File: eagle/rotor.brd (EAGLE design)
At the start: 72.1 x 80 mm, 53 parts, among them IC1 TXS0108, IC2 7815TV, J1 PL9823, J2 pwr2, J3 Power, J4 Antenna, J5 Power, J6 CCW, J7 Brake, J8 CW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

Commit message: eagle
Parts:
- J4: device TB004-508-02BE:CUI_TB004-508-02BE -> TB004-508-03BE:CUI_TB004-508-03BE
- Q1, T1: device test:TO92-EBC-OVAL -> test:TO92-CBE-OVAL
- R3: value 1100 -> 1100 Ω
- moved C4 7.41 mm to (63.5, 63.5)
- moved U3 6.35 mm to (62.2, 69.8)
- moved D1 6.35 mm to (62.2, 43.2), turned to 270 degrees
- moved J5 5.68 mm to (69.8, 12.7)
- moved J9 5.68 mm to (69.8, 22.9)
- moved R3 5.68 mm to (69.8, 64.8)
- moved T1 5.68 mm to (49.5, 19.1), turned to 270 degrees
- moved C5 4.58 mm to (66.0, 50.8)
- moved J7 3.81 mm to (49.5, 5.08)
- moved J1 3.81 mm to (24.1, 5.08)
- moved J6 3.81 mm to (59.7, 5.08)
- moved J8 3.81 mm to (39.4, 5.08)
- moved C1 3.59 mm to (54.6, 68.6)
- moved C3 3.59 mm to (54.6, 64.8)
- moved J3 3.59 mm to (22.9, 72.4)
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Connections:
- net +5V: now also Q1.C; no longer Q1.E
- net GND: now also J4.3
- net N$8: now also Q1.E; no longer Q1.C
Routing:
- net GND: track 241.7 -> 199.1 mm, vias 12 -> 11
- net N$1: track 33.7 -> 29.2 mm
- net SW1-POWER: track 60.2 -> 55.9 mm
- net ROTOR-PWR-LED-SOURCE: track 48.5 -> 44.1 mm
- net ROOF-3: track 23.2 -> 26.6 mm
- net SW4-CW: track 38.8 -> 36.1 mm
- net PL9823-SOURCE: track 37.0 -> 35.3 mm
- net +24: track 27.0 -> 28.5 mm
- net N$3: track 5.82 -> 7.18 mm
- net ROOF-4: track 23.4 -> 24.4 mm
- net SW3-BRAKE: track 42.2 -> 43.2 mm
- net CH0: track 34.3 -> 33.5 mm
- net POWER-OUT: track 51.6 -> 50.8 mm
- net +15V: track 32.3 -> 32.8 mm
- net SW2-CCW: track 52.0 -> 51.5 mm
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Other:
- board size 72.1 x 80 mm -> 74.9 x 77.5 mm

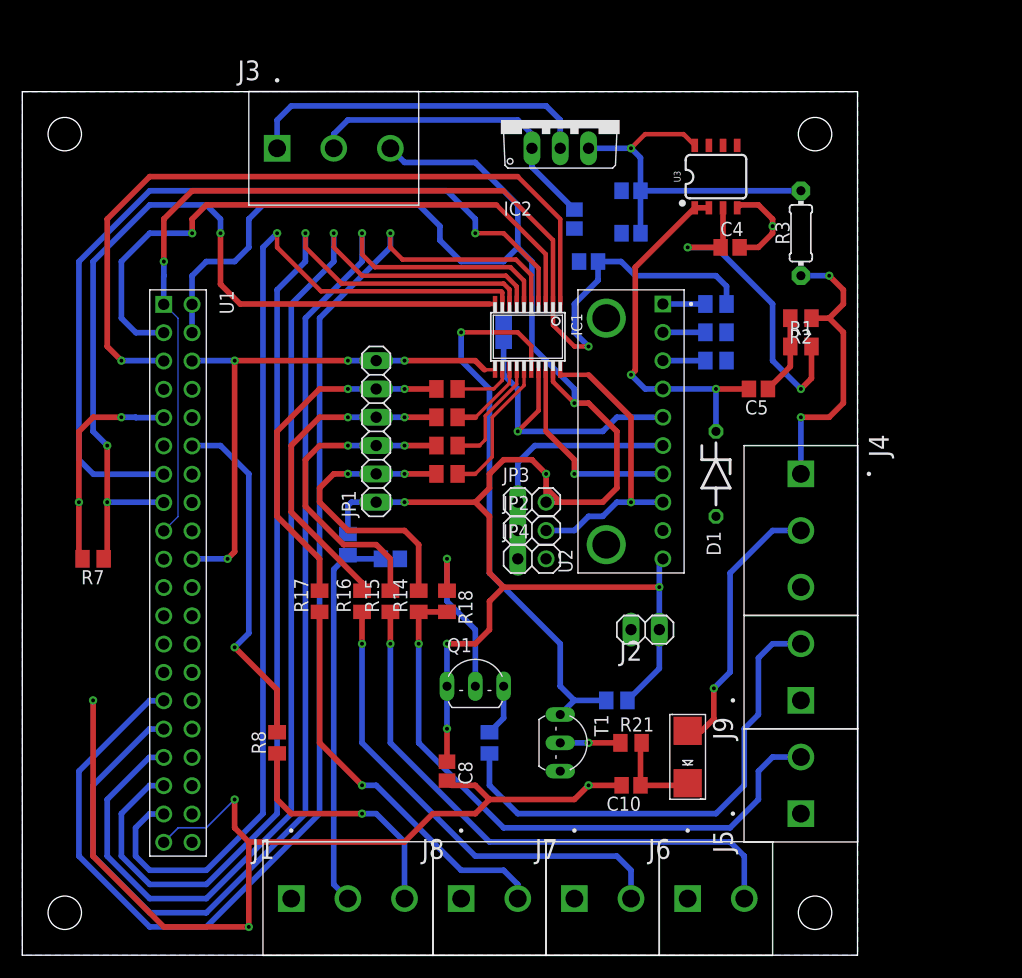
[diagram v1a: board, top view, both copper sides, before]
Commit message: add dpdt switch
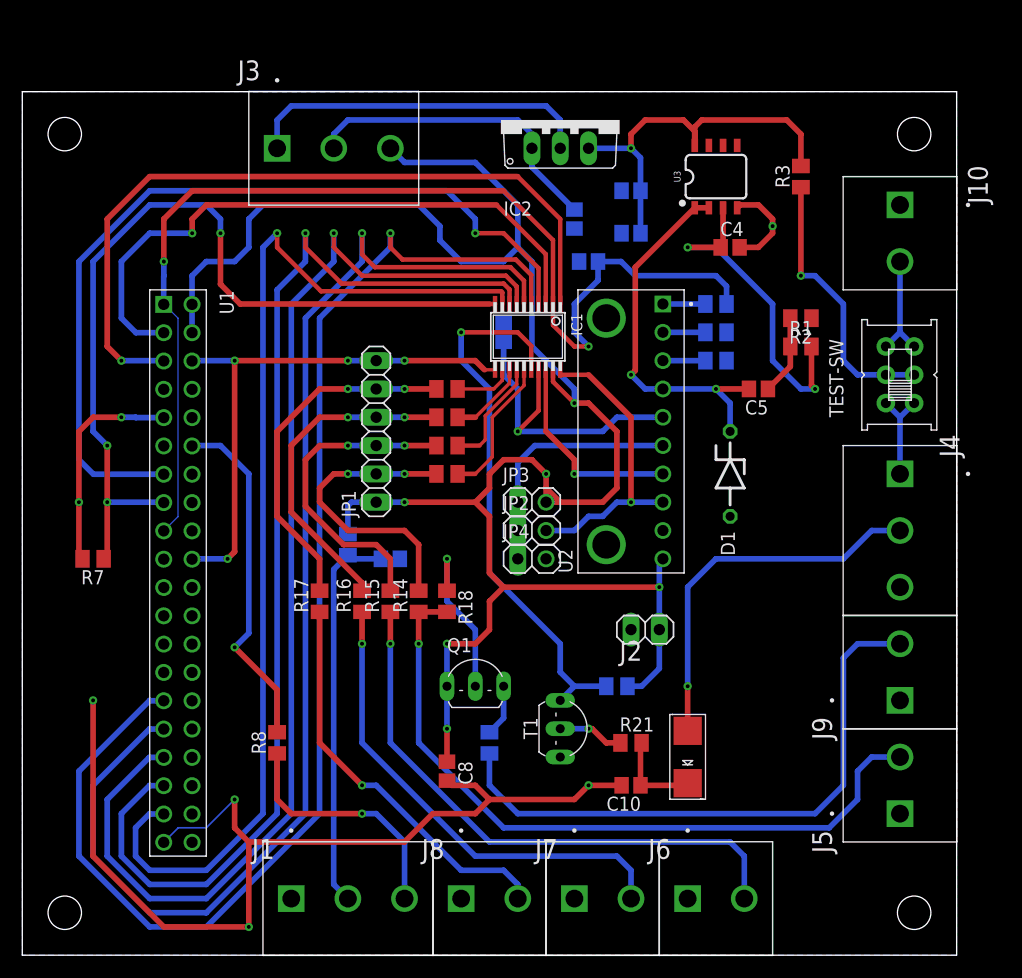
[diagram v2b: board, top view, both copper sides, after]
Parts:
- added J10: TB004-508-02BE, TB004-508-02BE:CUI_TB004-508-02BE
- added TEST-SW: DPDT-SWITCH, ladyada:DP-DT
- R3: device test:0204/7 -> ladyada:M0805
- moved J4 8.89 mm to (78.7, 43.2)
- moved J5 8.89 mm to (78.7, 12.7)
- moved J9 8.89 mm to (78.7, 22.9)
- moved R3 5.08 mm to (69.8, 69.8)
- moved D1 1.27 mm to (63.5, 43.2)
- moved R20 1.27 mm to (53.3, 24.1)
- moved T1 1.27 mm to (49.5, 20.3)
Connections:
- new net N$13: R3.1, TEST-SW.C-1, TEST-SW.C-2
- new net N$14: J10.2, TEST-SW.NC-1, TEST-SW.NC-2
- net GND: now also J10.1
- net ROOF-3: now also TEST-SW.NO-1, TEST-SW.NO-2; no longer R2.1, R3.1
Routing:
- net N$13: track 0.00 -> 24.8 mm, vias 0 -> 1
- net ROOF-3: track 26.6 -> 8.67 mm, vias 2 -> 0
- net N$14: track 0.00 -> 9.94 mm
- net ROTOR-PWR-LED-SOURCE: track 44.1 -> 53.8 mm
- net ROOF-4: track 24.4 -> 34.0 mm
- net SW1-POWER: track 55.9 -> 64.7 mm
- net +15V: track 32.8 -> 35.8 mm
- net POWER-OUT: track 50.8 -> 49.6 mm
- net N$1: track 29.2 -> 30.2 mm
- net CH0: track 33.5 -> 34.1 mm
- net +5V: track 179.4 -> 178.9 mm
- net N$12: track 5.40 -> 5.93 mm
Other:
- board size 74.9 x 77.5 mm -> 83.8 x 77.5 mm
